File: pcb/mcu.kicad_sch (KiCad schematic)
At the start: 26 parts, among them J3 Conn_01x06, U4 ESP32-C6-WROOM-1

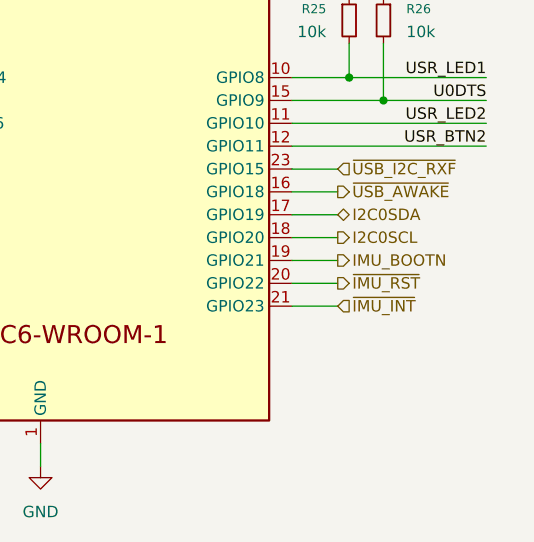
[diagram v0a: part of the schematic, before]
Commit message: [firmware/pcb] Initial firmware upload + fixed mistake in PCB + added errata documentation
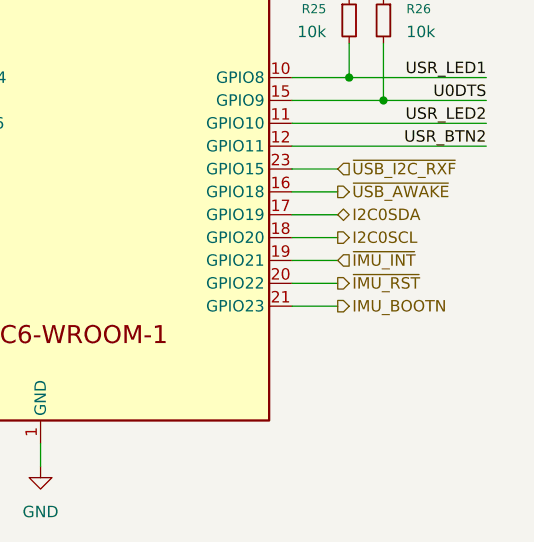
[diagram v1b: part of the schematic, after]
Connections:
- net IMU_BOOTN: now also U4.21 (GPIO23); no longer U4.19 (GPIO21)
- net ~{IMU_INT}: now also U4.19 (GPIO21); no longer U4.21 (GPIO23)
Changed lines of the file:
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@@
+	(wire
+		(pts
+			(xy 238.76 97.79) (xy 243.84 97.79)
+		)
+		(stroke
+			(width 0)
+			(type default)
+		)
+	)
 	(wire
 		(pts
@@
 	(wire
 		(pts
+			(xy 238.76 102.87) (xy 243.84 102.87)
+		)
+		(stroke
+			(width 0)
+			(type default)
+		)
+	)
+	(wire
+		(pts
 			(xy 73.66 115.57) (xy 78.74 115.57)
 		)
@@
 	(wire
 		(pts
-			(xy 238.76 97.79) (xy 243.84 97.79)
-		)
-		(stroke
-			(width 0)
-			(type default)
-		)
-	)
-	(wire
-		(pts
 			(xy 33.02 71.12) (xy 33.02 74.93)
 		)
@@
 		(pts
 			(xy 68.58 38.1) (xy 68.58 41.91)
-		)
-		(stroke
-			(width 0)
-			(type default)
-		)
-	)
-	(wire
-		(pts
-			(xy 238.76 102.87) (xy 243.84 102.87)
 		)
 		(stroke
@@
 	(hierarchical_label "IMU_BOOTN"
 		(shape output)
-		(at 243.84 97.79 0)
+		(at 243.84 102.87 0)
 		(effects
 			(font
@@
 	(hierarchical_label "~{IMU_INT}"
 		(shape input)
-		(at 243.84 102.87 0)
-		(effects
-			(font
+		(at 243.84 97.79 0)
+		(effects
+			(font
